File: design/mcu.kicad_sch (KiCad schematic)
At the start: 30 parts, among them J2 SWD_01X04, J3 DEBUG_SPI, U6 STM32H750VBTx, X1 ASTX-H11-25.000MHZ-T

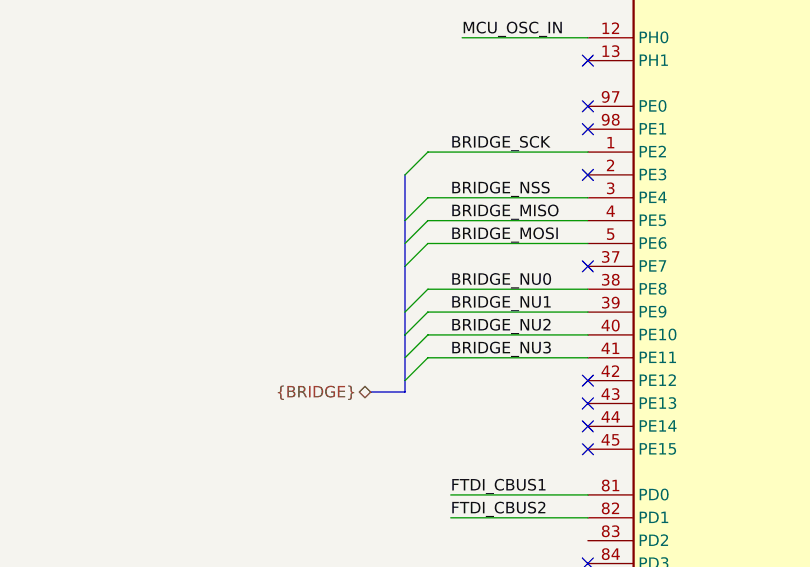
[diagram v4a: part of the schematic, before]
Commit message: Added FPGA LEDs layout
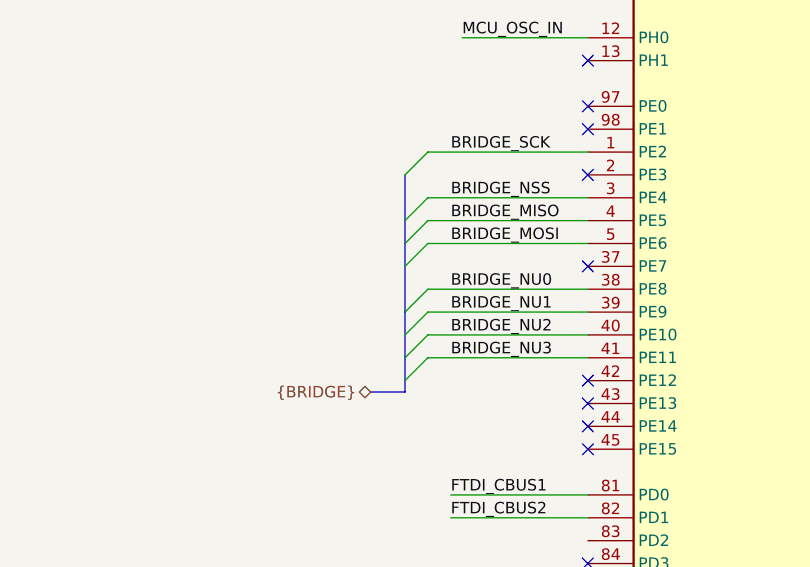
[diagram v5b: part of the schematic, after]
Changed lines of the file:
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@@
-(kicad_sch (version 20200512) (host eeschema "5.99.0-unknown-2cf82d9~101~ubuntu18.04.1")
-  (page 1 8)
+(kicad_sch (version 20200512) (host eeschema "5.99.0-unknown-ad88874~101~ubuntu18.04.1")
+  (page 3 8)
   (paper "A4")
   (title_block
@@
   (junction (at 236.22 25.4))
   (junction (at 262.89 26.67))
+  (no_connect (at 123.19 142.24))
+  (no_connect (at 168.91 119.38))
+  (no_connect (at 123.19 109.22))
+  (no_connect (at 168.91 48.26))
+  (no_connect (at 123.19 157.48))
+  (no_connect (at 168.91 154.94))
+  (no_connect (at 168.91 160.02))
+  (no_connect (at 168.91 114.3))
+  (no_connect (at 168.91 127))
+  (no_connect (at 168.91 142.24))
+  (no_connect (at 123.19 93.98))
+  (no_connect (at 168.91 66.04))
+  (no_connect (at 123.19 91.44))
+  (no_connect (at 168.91 101.6))
+  (no_connect (at 123.19 162.56))
+  (no_connect (at 168.91 63.5))
+  (no_connect (at 168.91 106.68))
+  (no_connect (at 168.91 121.92))
+  (no_connect (at 168.91 172.72))
+  (no_connect (at 168.91 55.88))
+  (no_connect (at 123.19 127))
+  (no_connect (at 168.91 60.96))
+  (no_connect (at 168.91 139.7))
+  (no_connect (at 168.91 116.84))
+  (no_connect (at 168.91 152.4))
+  (no_connect (at 168.91 144.78))
+  (no_connect (at 123.19 86.36))
+  (no_connect (at 168.91 124.46))
+  (no_connect (at 168.91 111.76))
+  (no_connect (at 123.19 154.94))
+  (no_connect (at 168.91 53.34))
+  (no_connect (at 123.19 160.02))
+  (no_connect (at 168.91 86.36))
+  (no_connect (at 168.91 167.64))
+  (no_connect (at 168.91 147.32))
+  (no_connect (at 123.19 121.92))
+  (no_connect (at 168.91 129.54))
+  (no_connect (at 168.91 134.62))
+  (no_connect (at 168.91 104.14))
+  (no_connect (at 123.19 99.06))
+  (no_connect (at 168.91 137.16))
   (no_connect (at 123.19 124.46))
-  (no_connect (at 123.19 93.98))
-  (no_connect (at 168.91 116.84))
-  (no_connect (at 168.91 144.78))
-  (no_connect (at 123.19 157.48))
-  (no_connect (at 168.91 101.6))
-  (no_connect (at 168.91 160.02))
-  (no_connect (at 168.91 48.26))
-  (no_connect (at 168.91 129.54))
+  (no_connect (at 123.19 129.54))
+  (no_connect (at 168.91 109.22))
+  (no_connect (at 168.91 149.86))
+  (no_connect (at 168.91 58.42))
   (no_connect (at 168.91 170.18))
-  (no_connect (at 123.19 142.24))
-  (no_connect (at 168.91 154.94))
-  (no_connect (at 168.91 134.62))
-  (no_connect (at 168.91 58.42))
-  (no_connect (at 123.19 121.92))
-  (no_connect (at 168.91 167.64))
-  (no_connect (at 168.91 124.46))
-  (no_connect (at 123.19 99.06))
-  (no_connect (at 168.91 104.14))
-  (no_connect (at 168.91 55.88))
-  (no_connect (at 168.91 60.96))
-  (no_connect (at 123.19 160.02))
-  (no_connect (at 168.91 172.72))
-  (no_connect (at 123.19 162.56))
-  (no_connect (at 123.19 86.36))
-  (no_connect (at 168.91 121.92))
+  (no_connect (at 168.91 50.8))
   (no_connect (at 168.91 68.58))
-  (no_connect (at 168.91 114.3))
-  (no_connect (at 168.91 86.36))
-  (no_connect (at 123.19 127))
-  (no_connect (at 168.91 66.04))
-  (no_connect (at 168.91 106.68))
-  (no_connect (at 168.91 139.7))
-  (no_connect (at 168.91 152.4))
-  (no_connect (at 168.91 149.86))
-  (no_connect (at 123.19 91.44))
-  (no_connect (at 168.91 137.16))
-  (no_connect (at 168.91 119.38))
-  (no_connect (at 168.91 63.5))
-  (no_connect (at 168.91 109.22))
-  (no_connect (at 168.91 53.34))
-  (no_connect (at 168.91 142.24))
-  (no_connect (at 123.19 154.94))
-  (no_connect (at 123.19 129.54))
-  (no_connect (at 168.91 147.32))
-  (no_connect (at 123.19 109.22))
-  (no_connect (at 168.91 127))
-  (no_connect (at 168.91 50.8))
-  (no_connect (at 168.91 111.76))
   (bus_entry (at 102.87 99.06) (size 2.54 -2.54))
   (bus_entry (at 102.87 104.14) (size 2.54 -2.54))
@@
   (wire (pts (xy 274.32 35.56) (xy 274.32 36.83)))
   (bus (pts (xy 99.06 123.19) (xy 102.87 123.19)))
-  (bus (pts (xy 102.87 99.06) (xy 102.87 104.14)))
-  (bus (pts (xy 102.87 104.14) (xy 102.87 109.22)))
-  (bus (pts (xy 102.87 109.22) (xy 102.87 116.84)))
-  (bus (pts (xy 102.87 116.84) (xy 102.87 121.92)))
-  (bus (pts (xy 102.87 121.92) (xy 102.87 123.19)))
+  (bus (pts (xy 102.87 99.06) (xy 102.87 106.68)))
+  (bus (pts (xy 102.87 106.68) (xy 102.87 114.3)))
+  (bus (pts (xy 102.87 114.3) (xy 102.87 119.38)))
+  (bus (pts (xy 102.87 119.38) (xy 102.87 123.19)))
   (bus (pts (xy 218.44 73.66) (xy 218.44 78.74)))
   (bus (pts (xy 218.44 78.74) (xy 218.44 93.98)))

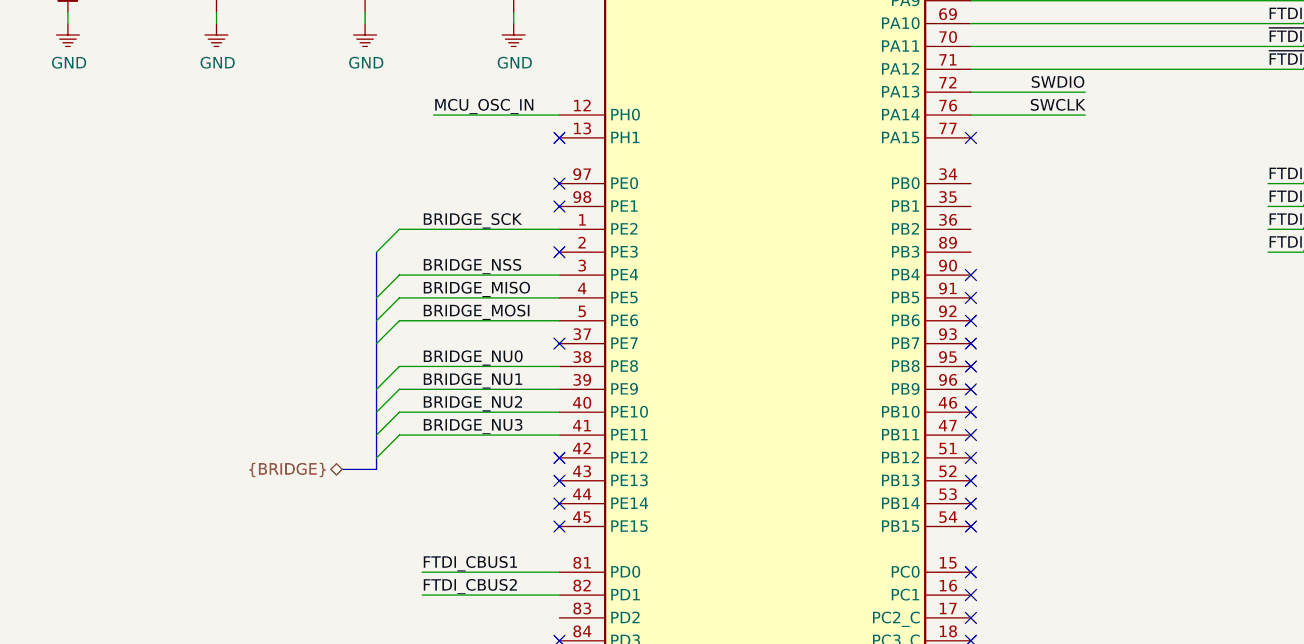
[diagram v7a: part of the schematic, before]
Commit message: Added bridge connection
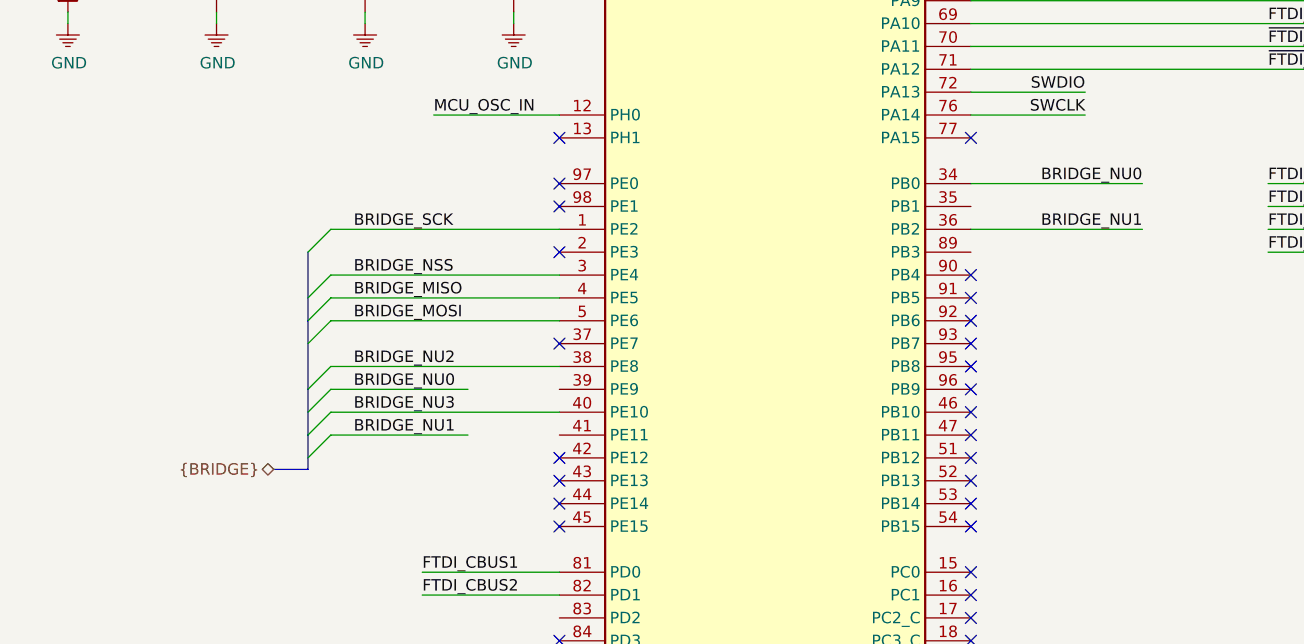
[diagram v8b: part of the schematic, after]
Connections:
- net BRIDGE_NU0: now also U6.34 (PB0); no longer U6.38 (PE8)
- net BRIDGE_NU1: now also U6.36 (PB2); no longer U6.39 (PE9)
- net BRIDGE_NU2: now also U6.38 (PE8); no longer U6.40 (PE10)
- net BRIDGE_NU3: now also U6.40 (PE10); no longer U6.41 (PE11)
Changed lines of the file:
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@@
   (no_connect (at 168.91 104.14))
   (no_connect (at 168.91 170.18))
-  (bus_entry (at 102.87 99.06) (size 2.54 -2.54))
-  (bus_entry (at 102.87 104.14) (size 2.54 -2.54))
-  (bus_entry (at 102.87 106.68) (size 2.54 -2.54))
-  (bus_entry (at 102.87 109.22) (size 2.54 -2.54))
-  (bus_entry (at 102.87 114.3) (size 2.54 -2.54))
-  (bus_entry (at 102.87 116.84) (size 2.54 -2.54))
-  (bus_entry (at 102.87 119.38) (size 2.54 -2.54))
-  (bus_entry (at 102.87 121.92) (size 2.54 -2.54))
+  (bus_entry (at 95.25 99.06) (size 2.54 -2.54))
+  (bus_entry (at 95.25 104.14) (size 2.54 -2.54))
+  (bus_entry (at 95.25 106.68) (size 2.54 -2.54))
+  (bus_entry (at 95.25 109.22) (size 2.54 -2.54))
+  (bus_entry (at 95.25 114.3) (size 2.54 -2.54))
+  (bus_entry (at 95.25 116.84) (size 2.54 -2.54))
+  (bus_entry (at 95.25 119.38) (size 2.54 -2.54))
+  (bus_entry (at 95.25 121.92) (size 2.54 -2.54))
   (bus_entry (at 218.44 73.66) (size -2.54 -2.54))
   (bus_entry (at 218.44 76.2) (size -2.54 -2.54))
@@
   (wire (pts (xy 93.98 172.72) (xy 86.36 172.72)))
   (wire (pts (xy 96.52 48.26) (xy 118.11 48.26)))
+  (wire (pts (xy 97.79 96.52) (xy 123.19 96.52)))
+  (wire (pts (xy 97.79 101.6) (xy 123.19 101.6)))
+  (wire (pts (xy 97.79 104.14) (xy 123.19 104.14)))
+  (wire (pts (xy 97.79 106.68) (xy 123.19 106.68)))
+  (wire (pts (xy 97.79 111.76) (xy 123.19 111.76)))
+  (wire (pts (xy 97.79 114.3) (xy 113.03 114.3)))
+  (wire (pts (xy 97.79 116.84) (xy 123.19 116.84)))
+  (wire (pts (xy 97.79 119.38) (xy 113.03 119.38)))
   (wire (pts (xy 100.33 60.96) (xy 101.6 60.96)))
   (wire (pts (xy 101.6 60.96) (xy 101.6 64.77)))
   (wire (pts (xy 101.6 60.96) (xy 123.19 60.96)))
   (wire (pts (xy 101.6 72.39) (xy 101.6 73.66)))
-  (wire (pts (xy 105.41 96.52) (xy 123.19 96.52)))
-  (wire (pts (xy 105.41 101.6) (xy 123.19 101.6)))
-  (wire (pts (xy 105.41 104.14) (xy 123.19 104.14)))
-  (wire (pts (xy 105.41 106.68) (xy 123.19 106.68)))
-  (wire (pts (xy 105.41 111.76) (xy 123.19 111.76)))
-  (wire (pts (xy 105.41 114.3) (xy 123.19 114.3)))
-  (wire (pts (xy 105.41 116.84) (xy 123.19 116.84)))
-  (wire (pts (xy 105.41 119.38) (xy 123.19 119.38)))
   (wire (pts (xy 107.95 134.62) (xy 123.19 134.62)))
   (wire (pts (xy 107.95 137.16) (xy 123.19 137.16)))
@@
   (wire (pts (xy 168.91 81.28) (xy 181.61 81.28)))
   (wire (pts (xy 168.91 83.82) (xy 181.61 83.82)))
+  (wire (pts (xy 168.91 91.44) (xy 187.96 91.44)))
+  (wire (pts (xy 168.91 96.52) (xy 187.96 96.52)))
   (wire (pts (xy 168.91 157.48) (xy 176.53 157.48)))
   (wire (pts (xy 168.91 162.56) (xy 184.15 162.56)))
@@
   (wire (pts (xy 274.32 26.67) (xy 274.32 27.94)))
   (wire (pts (xy 274.32 35.56) (xy 274.32 36.83)))
-  (bus (pts (xy 99.06 123.19) (xy 102.87 123.19)))
-  (bus (pts (xy 102.87 99.06) (xy 102.87 106.68)))
-  (bus (pts (xy 102.87 106.68) (xy 102.87 114.3)))
-  (bus (pts (xy 102.87 114.3) (xy 102.87 119.38)))
-  (bus (pts (xy 102.87 119.38) (xy 102.87 123.19)))
+  (bus (pts (xy 91.44 123.19) (xy 95.25 123.19)))
+  (bus (pts (xy 95.25 99.06) (xy 95.25 106.68)))
+  (bus (pts (xy 95.25 106.68) (xy 95.25 114.3)))
+  (bus (pts (xy 95.25 114.3) (xy 95.25 119.38)))
+  (bus (pts (xy 95.25 119.38) (xy 95.25 123.19)))
   (bus (pts (xy 218.44 73.66) (xy 218.44 78.74)))
   (bus (pts (xy 218.44 78.74) (xy 218.44 93.98)))
@@
     (effects (font (size 1.27 1.27)) (justify right bottom))
   )
+  (label "BRIDGE_SCK" (at 100.33 96.52 0)
+    (effects (font (size 1.27 1.27)) (justify left bottom))
+  )
+  (label "BRIDGE_NSS" (at 100.33 101.6 0)
+    (effects (font (size 1.27 1.27)) (justify left bottom))
+  )
+  (label "BRIDGE_MISO" (at 100.33 104.14 0)
+    (effects (font (size 1.27 1.27)) (justify left bottom))
+  )
+  (label "BRIDGE_MOSI" (at 100.33 106.68 0)
+    (effects (font (size 1.27 1.27)) (justify left bottom))
+  )
+  (label "BRIDGE_NU2" (at 100.33 111.76 0)
+    (effects (font (size 1.27 1.27)) (justify left bottom))
+  )
+  (label "BRIDGE_NU0" (at 100.33 114.3 0)
+    (effects (font (size 1.27 1.27)) (justify left bottom))
+  )
+  (label "BRIDGE_NU3" (at 100.33 116.84 0)
+    (effects (font (size 1.27 1.27)) (justify left bottom))
+  )
+  (label "BRIDGE_NU1" (at 100.33 119.38 0)
+    (effects (font (size 1.27 1.27)) (justify left bottom))
+  )
   (label "~RST" (at 101.6 48.26 0)
     (effects (font (size 1.27 1.27)) (justify left bottom))
@@
     (effects (font (size 1.27 1.27)) (justify left bottom))
   )
-  (label "BRIDGE_SCK" (at 107.95 96.52 0)
-    (effects (font (size 1.27 1.27)) (justify left bottom))
-  )
-  (label "BRIDGE_NSS" (at 107.95 101.6 0)
-    (effects (font (size 1.27 1.27)) (justify left bottom))
-  )
-  (label "BRIDGE_MISO" (at 107.95 104.14 0)
-    (effects (font (size 1.27 1.27)) (justify left bottom))
-  )
-  (label "BRIDGE_MOSI" (at 107.95 106.68 0)
-    (effects (font (size 1.27 1.27)) (justify left bottom))
-  )
-  (label "BRIDGE_NU0" (at 107.95 111.76 0)
-    (effects (font (size 1.27 1.27)) (justify left bottom))
-  )
-  (label "BRIDGE_NU1" (at 107.95 114.3 0)
-    (effects (font (size 1.27 1.27)) (justify left bottom))
-  )
-  (label "BRIDGE_NU2" (at 107.95 116.84 0)
-    (effects (font (size 1.27 1.27)) (justify left bottom))
-  )
-  (label "BRIDGE_NU3" (at 107.95 119.38 0)
-    (effects (font (size 1.27 1.27)) (justify left bottom))
-  )
   (label "FTDI_CBUS1" (at 107.95 134.62 0)
     (effects (font (size 1.27 1.27)) (justify left bottom))
@@
     (effects (font (size 1.27 1.27)) (justify right bottom))
   )
+  (label "BRIDGE_NU0" (at 187.96 91.44 180)
+    (effects (font (size 1.27 1.27)) (justify right bottom))
+  )
+  (label "BRIDGE_NU1" (at 187.96 96.52 180)
+    (effects (font (size 1.27 1.27)) (justify right bottom))
+  )
   (label "RCC_MCO2" (at 199.39 157.48 180)
     (effects (font (size 1.27 1.27)) (justify right bottom))
@@
   (label "FPGA_LOAD_BITSTREAM" (at 237.49 130.81 0)
     (effects (font (size 1.27 1.27)) (justify left bottom))
+  )
+  (hierarchical_label "{BRIDGE}" (shape bidirectional) (at 91.44 123.19 180)
+    (effects (font (size 1.27 1.27)) (justify right))
   )
   (hierarchical_label "~RST" (shape input) (at 96.52 48.26 180)
     (effects (font (size 1.27 1.27)) (justify right))
   )
-  (hierarchical_label "{BRIDGE}" (shape bidirectional) (at 99.06 123.19 180)
-    (effects (font (size 1.27 1.27)) (justify right))
-  )
